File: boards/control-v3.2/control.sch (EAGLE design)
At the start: 109 parts, among them IC1 MCP23017-E/SS, J1 2-PIN-KICKERS, J3 HFW8R-1ST, J4 4-PIN-HEADER, J6 DF22-2, U1 XC3S250E-4TQG144C, U11 MCP1824T-1202E/OT, U12 MCP1824T-2502E/OT, U13 TLV70233DBVR, U4 ICM-42605, U5 SN74AHC1G125, U7 MPM3620GQV-P, U8 VND5E006ASPTR-E, X1 ASV-18.432MHZ-EJ-T

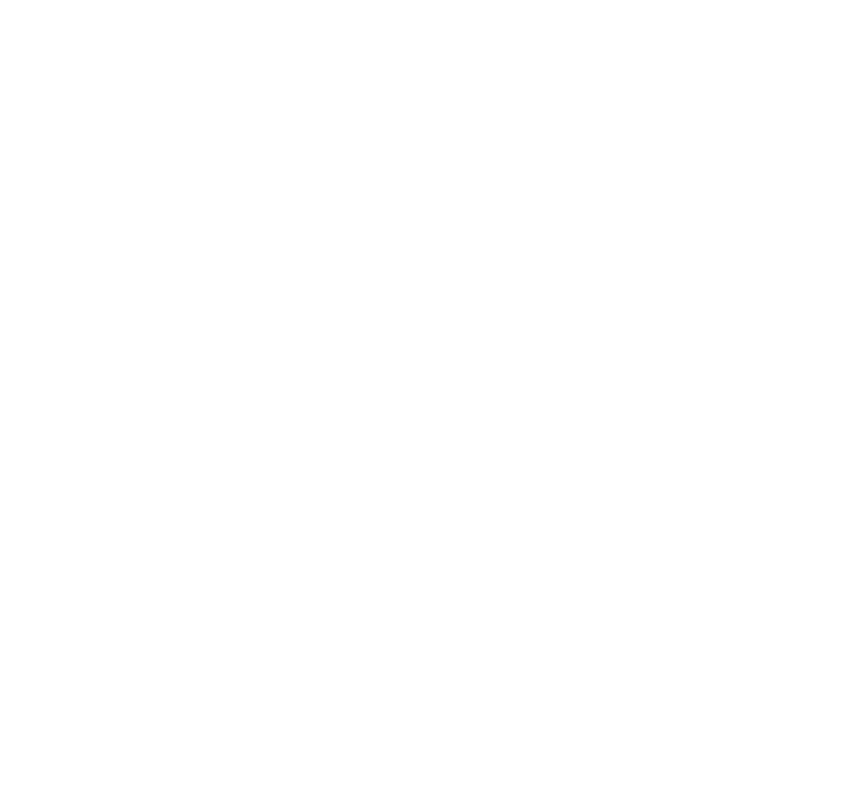
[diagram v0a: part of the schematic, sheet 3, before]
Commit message: Added RST network
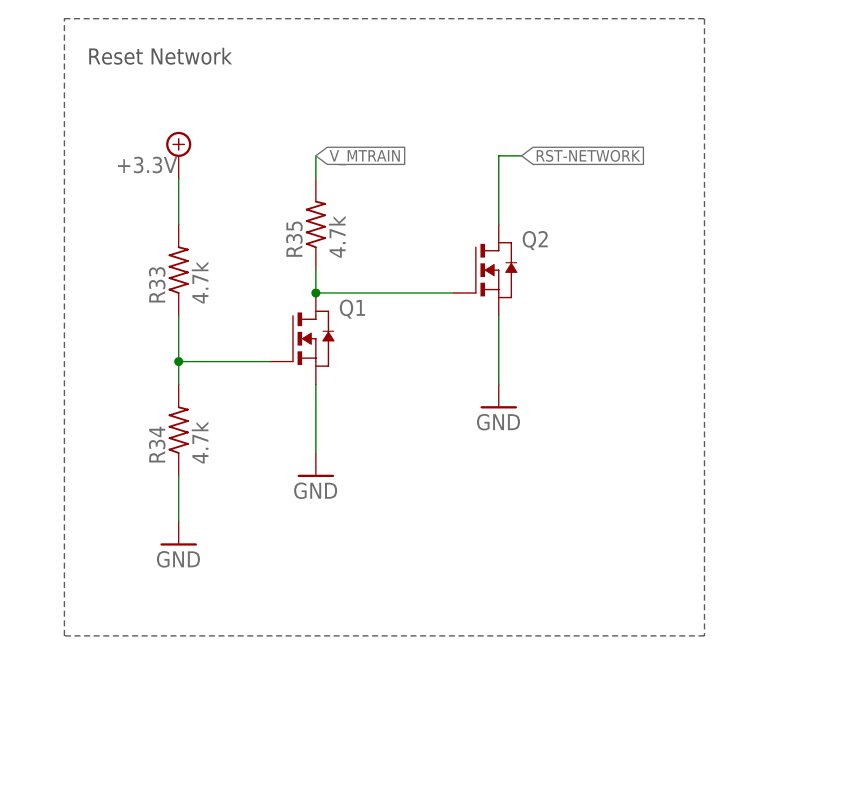
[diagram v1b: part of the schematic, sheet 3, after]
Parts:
- added Q1, Q2: (no value), RoboJackets-Discrete:NMOSSOT-23-3
- added R33, R34, R35: 4.7k, resistor:R-US_R0603
- R1: value 68k -> 68k 1%
- R2, R3, R4: value 10k -> 10k 1%
- R26, R27, R28, R29: value 0k -> 0
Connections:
- new net N$3: Q1.D, Q2.G, R35.1
- new net RST-NETWORK: KIT1.!RST, Q2.D
- new net V_MTRAIN: KIT1.VDD, R35.2, R5.1
- net +18.5V: now also Q1.D
- net +3.3V: now also R33.2; no longer KIT1.VDD, R5.1
- net GH-A: now also Q1.G
- net GL-A: now also Q2.G
- net GND: now also Q1.S, Q2.S, R34.1
- net N$1: now also Q1.G, R33.1, R34.2; no longer KIT1.VBUS
- net PHASE-A: now also Q1.S, Q2.D
- net PHASE-B: now also Q1.S, Q2.D
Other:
- note added: "Reset Network"

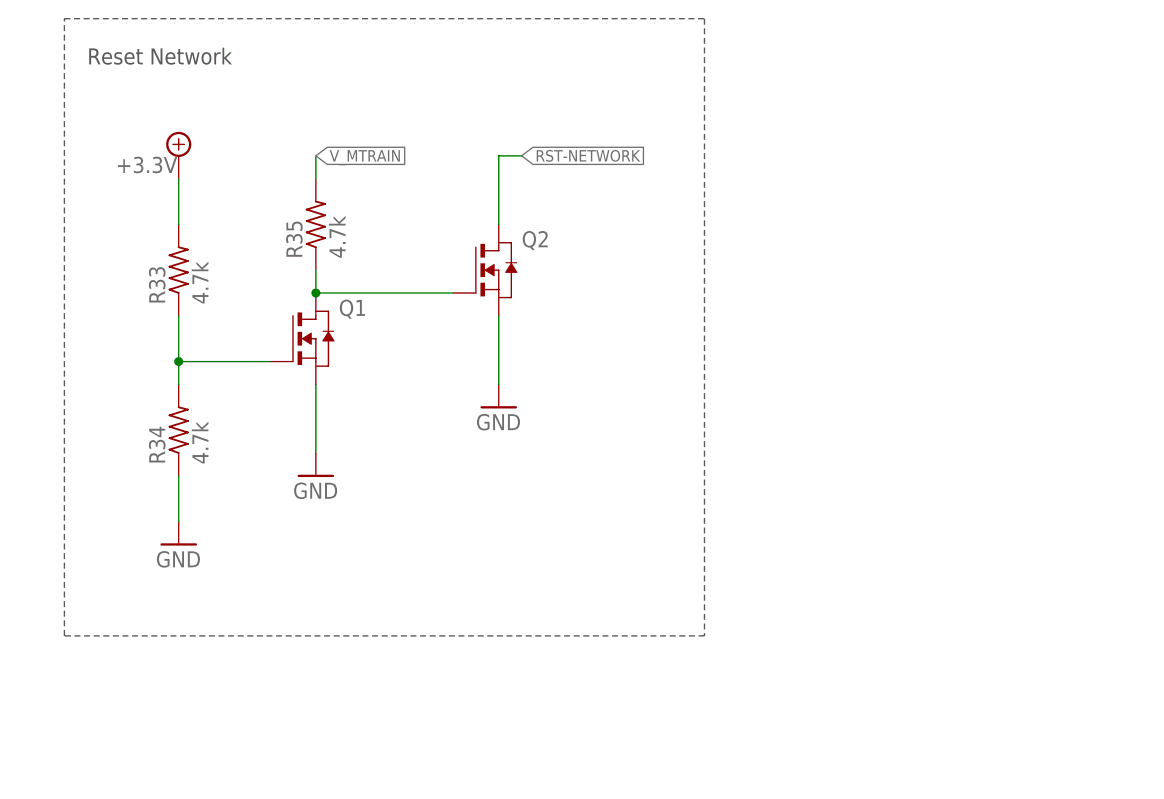
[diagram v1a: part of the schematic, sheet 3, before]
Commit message: Fixed RST network
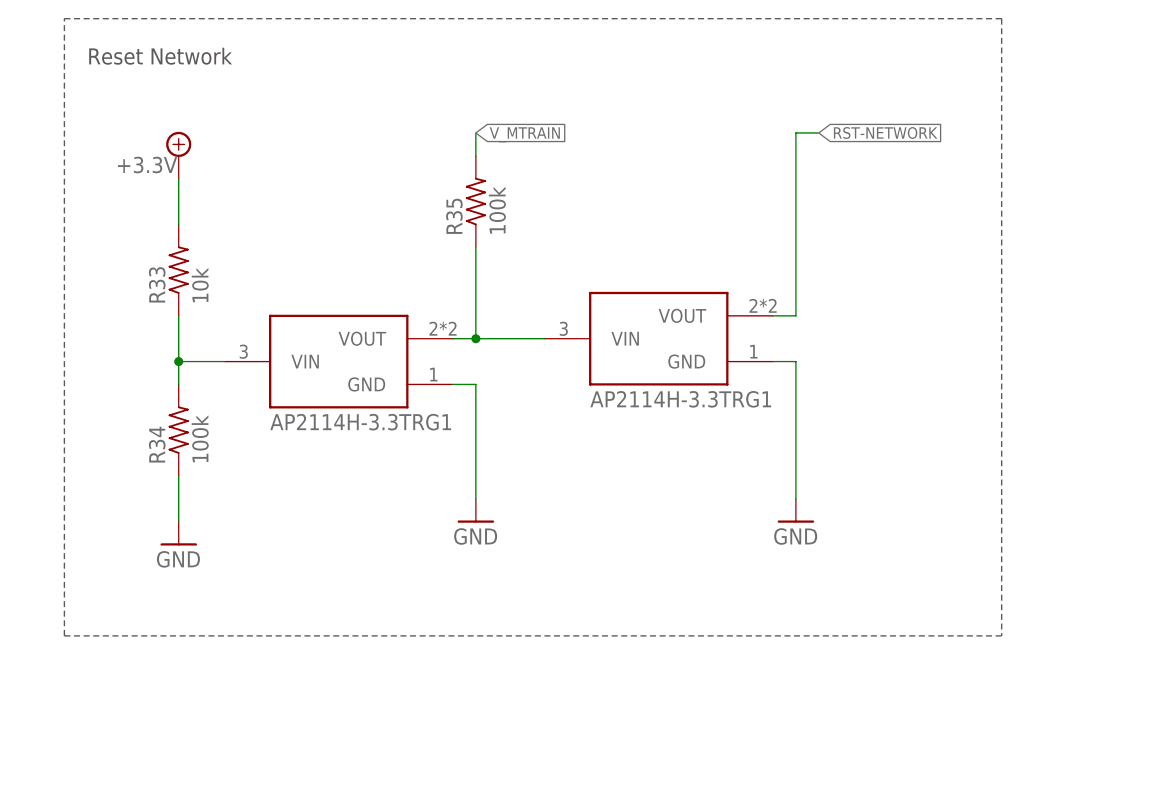
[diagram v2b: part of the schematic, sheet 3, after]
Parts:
- removed D1: GREEN, RoboJackets-LEDs:LED-SMD-GREEN
- removed Q1, Q2: (no value), RoboJackets-Discrete:NMOSSOT-23-3
- removed R5: 330, resistor:R-US_R0603
- added U$16, U$17: AP2114H-3.3TRG1, RoboJackets-PowerICs:AP2114H-3.3TRG1
- R33: value 4.7k -> 10k
- R34, R35: value 4.7k -> 100k
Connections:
- removed net VDD-LED: D1.A, R5.2
- net +18.5V: no longer Q1.D
- net GH-A: no longer Q1.G
- net GL-A: no longer Q2.G
- net GND: now also U$16.GND, U$17.GND; no longer D1.K, Q1.S, Q2.S
- net N$1: now also U$16.VIN; no longer Q1.G
- net N$3: now also U$16.VOUT, U$17.VIN; no longer Q1.D, Q2.G
- net PHASE-A: no longer Q1.S, Q2.D
- net PHASE-B: no longer Q1.S, Q2.D
- net RST-NETWORK: now also U$17.VOUT; no longer Q2.D
- net V_MTRAIN: no longer R5.1
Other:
- moved on the sheet: R35

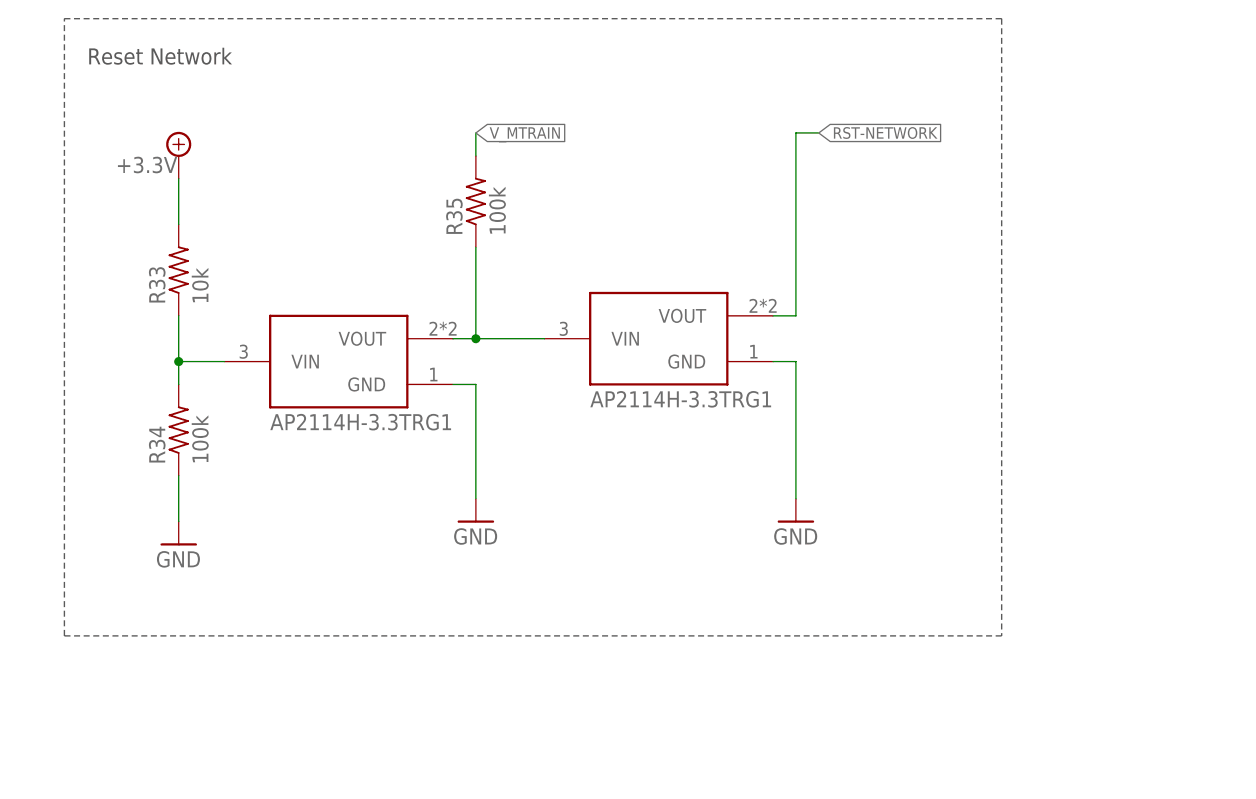
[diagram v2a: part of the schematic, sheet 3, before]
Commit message: reset FET fixes
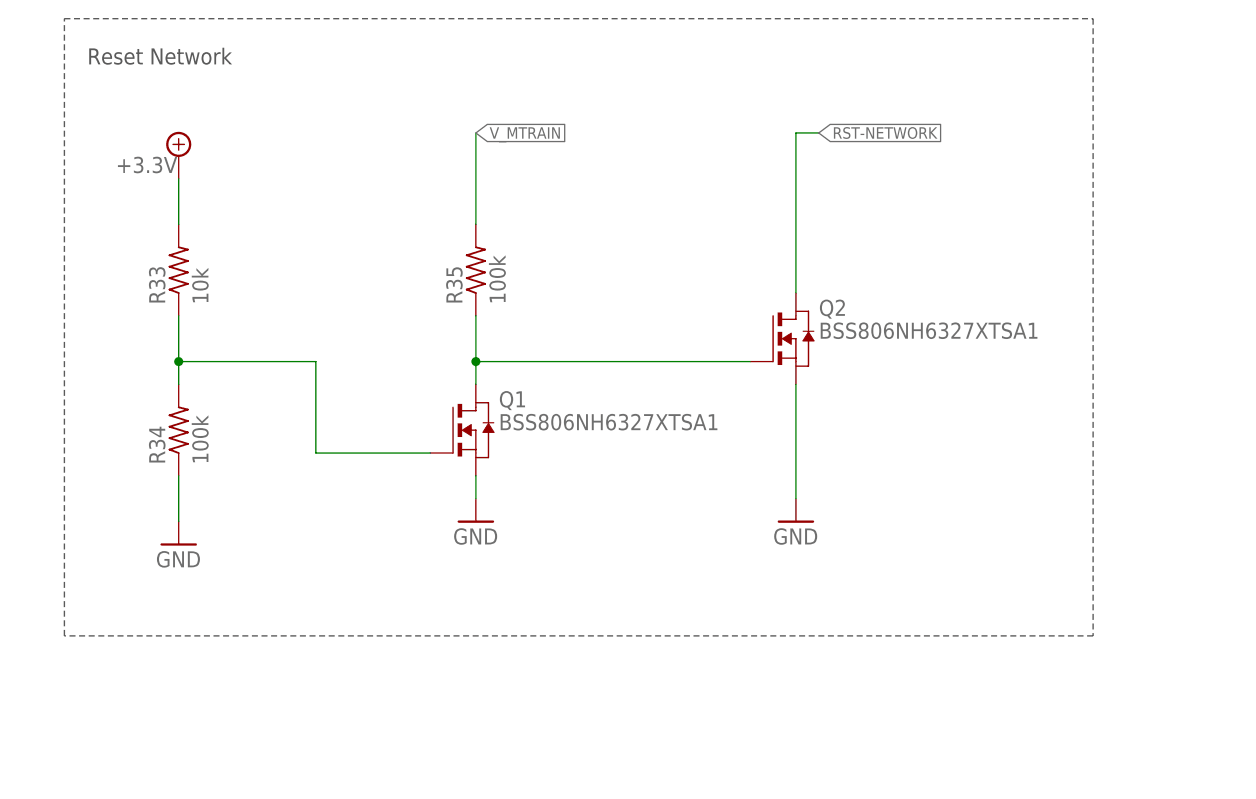
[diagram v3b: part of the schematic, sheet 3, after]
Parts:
- removed U$16, U$17: AP2114H-3.3TRG1, RoboJackets-PowerICs:AP2114H-3.3TRG1
- added Q1, Q2: BSS806NH6327XTSA1, RoboJackets-Discrete:NMOSSOT-23-3
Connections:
- net +18.5V: now also Q1.D
- net GH-A: now also Q1.G
- net GL-A: now also Q2.G
- net GND: now also Q1.S, Q2.S; no longer U$16.GND, U$17.GND
- net N$1: now also Q1.G; no longer U$16.VIN
- net N$3: now also Q1.D, Q2.G; no longer U$16.VOUT, U$17.VIN
- net PHASE-A: now also Q1.S, Q2.D
- net PHASE-B: now also Q1.S, Q2.D
- net RST-NETWORK: now also Q2.D; no longer U$17.VOUT
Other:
- moved on the sheet: R35
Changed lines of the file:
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@@
 <?xml version="1.0" encoding="utf-8"?>
 <!DOCTYPE eagle SYSTEM "eagle.dtd">
-<eagle version="9.1.3">
+<eagle version="9.4.2">
 <drawing>
 <settings>
@@
 <part name="GND39" library="supply1" deviceset="GND" device=""/>
 <part name="GND40" library="supply1" deviceset="GND" device=""/>
-<part name="U$16" library="RoboJackets-PowerICs" deviceset="AP2114H" device="" technology="-3.3TRG1"/>
-<part name="U$17" library="RoboJackets-PowerICs" deviceset="AP2114H" device="" technology="-3.3TRG1"/>
+<part name="Q1" library="RoboJackets-Discrete" deviceset="NMOS" device="SOT-23-3" value="BSS806NH6327XTSA1"/>
+<part name="Q2" library="RoboJackets-Discrete" deviceset="NMOS" device="SOT-23-3" value="BSS806NH6327XTSA1"/>
 </parts>
 <sheets>
@@
 <wire x1="7.62" y1="5.08" x2="7.62" y2="88.9" width="0.1524" layer="97" style="shortdash"/>
 <text x="10.16" y="83.82" size="1.778" layer="97">IO Expander</text>
-<wire x1="12.7" y1="198.12" x2="116.84" y2="198.12" width="0.1524" layer="97" style="shortdash"/>
-<wire x1="116.84" y1="198.12" x2="116.84" y2="129.54" width="0.1524" layer="97" style="shortdash"/>
-<wire x1="116.84" y1="129.54" x2="12.7" y2="129.54" width="0.1524" layer="97" style="shortdash"/>
+<wire x1="12.7" y1="198.12" x2="127" y2="198.12" width="0.1524" layer="97" style="shortdash"/>
+<wire x1="127" y1="198.12" x2="127" y2="129.54" width="0.1524" layer="97" style="shortdash"/>
+<wire x1="127" y1="129.54" x2="12.7" y2="129.54" width="0.1524" layer="97" style="shortdash"/>
 <wire x1="12.7" y1="129.54" x2="12.7" y2="198.12" width="0.1524" layer="97" style="shortdash"/>
 <text x="15.24" y="193.04" size="1.778" layer="97">Reset Network</text>
@@
 <attribute name="VALUE" x="28.702" y="148.59" size="1.778" layer="96" rot="R90"/>
 </instance>
-<instance part="R35" gate="G$1" x="58.42" y="177.8" smashed="yes" rot="R90">
-<attribute name="NAME" x="56.9214" y="173.99" size="1.778" layer="95" rot="R90"/>
-<attribute name="VALUE" x="61.722" y="173.99" size="1.778" layer="96" rot="R90"/>
+<instance part="R35" gate="G$1" x="58.42" y="170.18" smashed="yes" rot="R90">
+<attribute name="NAME" x="56.9214" y="166.37" size="1.778" layer="95" rot="R90"/>
+<attribute name="VALUE" x="61.722" y="166.37" size="1.778" layer="96" rot="R90"/>
 </instance>
 <instance part="SUPPLY4" gate="P" x="25.4" y="182.88" smashed="yes">
@@
 <attribute name="VALUE" x="91.44" y="139.7" size="1.778" layer="96"/>
 </instance>
-<instance part="U$16" gate="G$1" x="43.18" y="160.02"/>
-<instance part="U$17" gate="G$1" x="78.74" y="162.56"/>
+<instance part="Q1" gate="G$1" x="58.42" y="152.4" smashed="yes">
+<attribute name="VALUE" x="60.96" y="152.4" size="1.778" layer="96"/>
+<attribute name="NAME" x="60.96" y="154.94" size="1.778" layer="95"/>
+</instance>
+<instance part="Q2" gate="G$1" x="93.98" y="162.56" smashed="yes">
+<attribute name="VALUE" x="96.52" y="162.56" size="1.778" layer="96"/>
+<attribute name="NAME" x="96.52" y="165.1" size="1.778" layer="95"/>
+</instance>
 </instances>
 <busses>
@@
 </segment>
 <segment>
-<pinref part="U$16" gate="G$1" pin="GND"/>
 <pinref part="GND39" gate="1" pin="GND"/>
-<wire x1="55.88" y1="157.48" x2="58.42" y2="157.48" width="0.1524" layer="91"/>
-<wire x1="58.42" y1="157.48" x2="58.42" y2="144.78" width="0.1524" layer="91"/>
+<wire x1="58.42" y1="147.32" x2="58.42" y2="144.78" width="0.1524" layer="91"/>
+<pinref part="Q1" gate="G$1" pin="S"/>
 </segment>
 <segment>
-<pinref part="U$17" gate="G$1" pin="GND"/>
 <pinref part="GND40" gate="1" pin="GND"/>
-<wire x1="91.44" y1="160.02" x2="93.98" y2="160.02" width="0.1524" layer="91"/>
-<wire x1="93.98" y1="160.02" x2="93.98" y2="144.78" width="0.1524" layer="91"/>
+<wire x1="93.98" y1="157.48" x2="93.98" y2="144.78" width="0.1524" layer="91"/>
+<pinref part="Q2" gate="G$1" pin="S"/>
 </segment>
 </net>
@@
 <wire x1="25.4" y1="157.48" x2="25.4" y2="160.02" width="0.1524" layer="91"/>
 <wire x1="25.4" y1="160.02" x2="25.4" y2="165.1" width="0.1524" layer="91"/>
-<pinref part="U$16" gate="G$1" pin="VIN"/>
-<wire x1="30.48" y1="160.02" x2="25.4" y2="160.02" width="0.1524" layer="91"/>
 <junction x="25.4" y="160.02"/>
+<wire x1="25.4" y1="160.02" x2="40.64" y2="160.02" width="0.1524" layer="91"/>
+<pinref part="Q1" gate="G$1" pin="G"/>
+<wire x1="40.64" y1="160.02" x2="40.64" y2="149.86" width="0.1524" layer="91"/>
+<wire x1="40.64" y1="149.86" x2="53.34" y2="149.86" width="0.1524" layer="91"/>
 </segment>
 </net>
@@
 <wire x1="93.98" y1="185.42" x2="96.52" y2="185.42" width="0.1524" layer="91"/>
 <label x="96.52" y="185.42" size="1.27" layer="95" xref="yes"/>
-<pinref part="U$17" gate="G$1" pin="VOUT"/>
-<wire x1="91.44" y1="165.1" x2="93.98" y2="165.1" width="0.1524" layer="91"/>
-<wire x1="93.98" y1="165.1" x2="93.98" y2="185.42" width="0.1524" layer="91"/>
+<wire x1="93.98" y1="167.64" x2="93.98" y2="185.42" width="0.1524" layer="91"/>
+<pinref part="Q2" gate="G$1" pin="D"/>
 </segment>
 </net>
@@
 <segment>
 <pinref part="R35" gate="G$1" pin="2"/>
-<wire x1="58.42" y1="182.88" x2="58.42" y2="185.42" width="0.1524" layer="91"/>
+<wire x1="58.42" y1="175.26" x2="58.42" y2="185.42" width="0.1524" layer="91"/>
 <label x="58.42" y="185.42" size="1.27" layer="95" xref="yes"/>
 </segment>
@@
 <segment>
 <pinref part="R35" gate="G$1" pin="1"/>
-<pinref part="U$16" gate="G$1" pin="VOUT"/>
-<wire x1="58.42" y1="172.72" x2="58.42" y2="162.56" width="0.1524" layer="91"/>
-<wire x1="58.42" y1="162.56" x2="55.88" y2="162.56" width="0.1524" layer="91"/>
-<pinref part="U$17" gate="G$1" pin="VIN"/>
-<wire x1="58.42" y1="162.56" x2="66.04" y2="162.56" width="0.1524" layer="91"/>
-<junction x="58.42" y="162.56"/>
+<wire x1="58.42" y1="165.1" x2="58.42" y2="160.02" width="0.1524" layer="91"/>
+<pinref part="Q1" gate="G$1" pin="D"/>
+<pinref part="Q2" gate="G$1" pin="G"/>
+<wire x1="58.42" y1="160.02" x2="58.42" y2="157.48" width="0.1524" layer="91"/>
+<wire x1="88.9" y1="160.02" x2="58.42" y2="160.02" width="0.1524" layer="91"/>
+<junction x="58.42" y="160.02"/>
 </segment>
 </net>
@@
 <attribute name="NAME" x="50.8" y="165.1" size="2.032" layer="95" align="bottom-center"/>
 <attribute name="NAME" x="50.8" y="165.1" size="2.032" layer="95" align="bottom-center"/>
+<attribute name="NAME" x="50.8" y="165.1" size="2.032" layer="95" align="bottom-center"/>
 </moduleinst>
 <moduleinst name="M2" module="WHEEL_DRIVE" x="50.8" y="86.36">
@@
 <attribute name="NAME" x="50.8" y="86.36" size="2.032" layer="95" align="bottom-center"/>
 <attribute name="NAME" x="50.8" y="86.36" size="2.032" layer="95" align="bottom-center"/>
+<attribute name="NAME" x="50.8" y="86.36" size="2.032" layer="95" align="bottom-center"/>
 </moduleinst>
 <moduleinst name="M3" module="WHEEL_DRIVE" x="228.6" y="86.36">
@@
 <attribute name="NAME" x="228.6" y="86.36" size="2.032" layer="95" align="bottom-center"/>
 <attribute name="NAME" x="228.6" y="86.36" size="2.032" layer="95" align="bottom-center"/>
+<attribute name="NAME" x="228.6" y="86.36" size="2.032" layer="95" align="bottom-center"/>
 </moduleinst>
 <moduleinst name="M4" module="WHEEL_DRIVE" x="228.6" y="165.1">
@@
 <attribute name="NAME" x="228.6" y="165.1" size="2.032" layer="95" align="bottom-center"/>
 <attribute name="NAME" x="228.6" y="165.1" size="2.032" layer="95" align="bottom-center"/>
+<attribute name="NAME" x="228.6" y="165.1" size="2.032" layer="95" align="bottom-center"/>
 </moduleinst>
 <moduleinst name="DD" module="DRIBBLER_DRIVE" x="144.78" y="165.1">
 <attribute name="NAME" x="144.78" y="165.1" size="2.032" layer="95" align="bottom-center"/>
 <attribute name="NAME" x="144.78" y="165.1" size="2.032" layer="95" align="bottom-center"/>
+<attribute name="NAME" x="144.78" y="165.1" size="2.032" layer="95" align="bottom-center"/>
